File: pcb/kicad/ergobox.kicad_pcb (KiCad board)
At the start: 2 copper layers, 236 x 147 mm, 79 parts, among them SW1 SW_Push, SW10 Kailh, SW11 Kailh, SW12 Kailh, SW13 Kailh, SW14 Kailh, SW15 Kailh, SW16 Kailh, SW17 Kailh, SW18 Kailh, SW19 Kailh, SW2 SW_Push, SW20 Kailh, SW3 SW_Push, SW4 SW_Push, SW5 SW_Push, SW6 SW_Push, SW7 SW_Push, SW8 SW_Push, SW9 Kailh, U1 TLV73333PDBV, U2 RP2040, U3 W25Q128JVS, Y1 Crystal_GND24

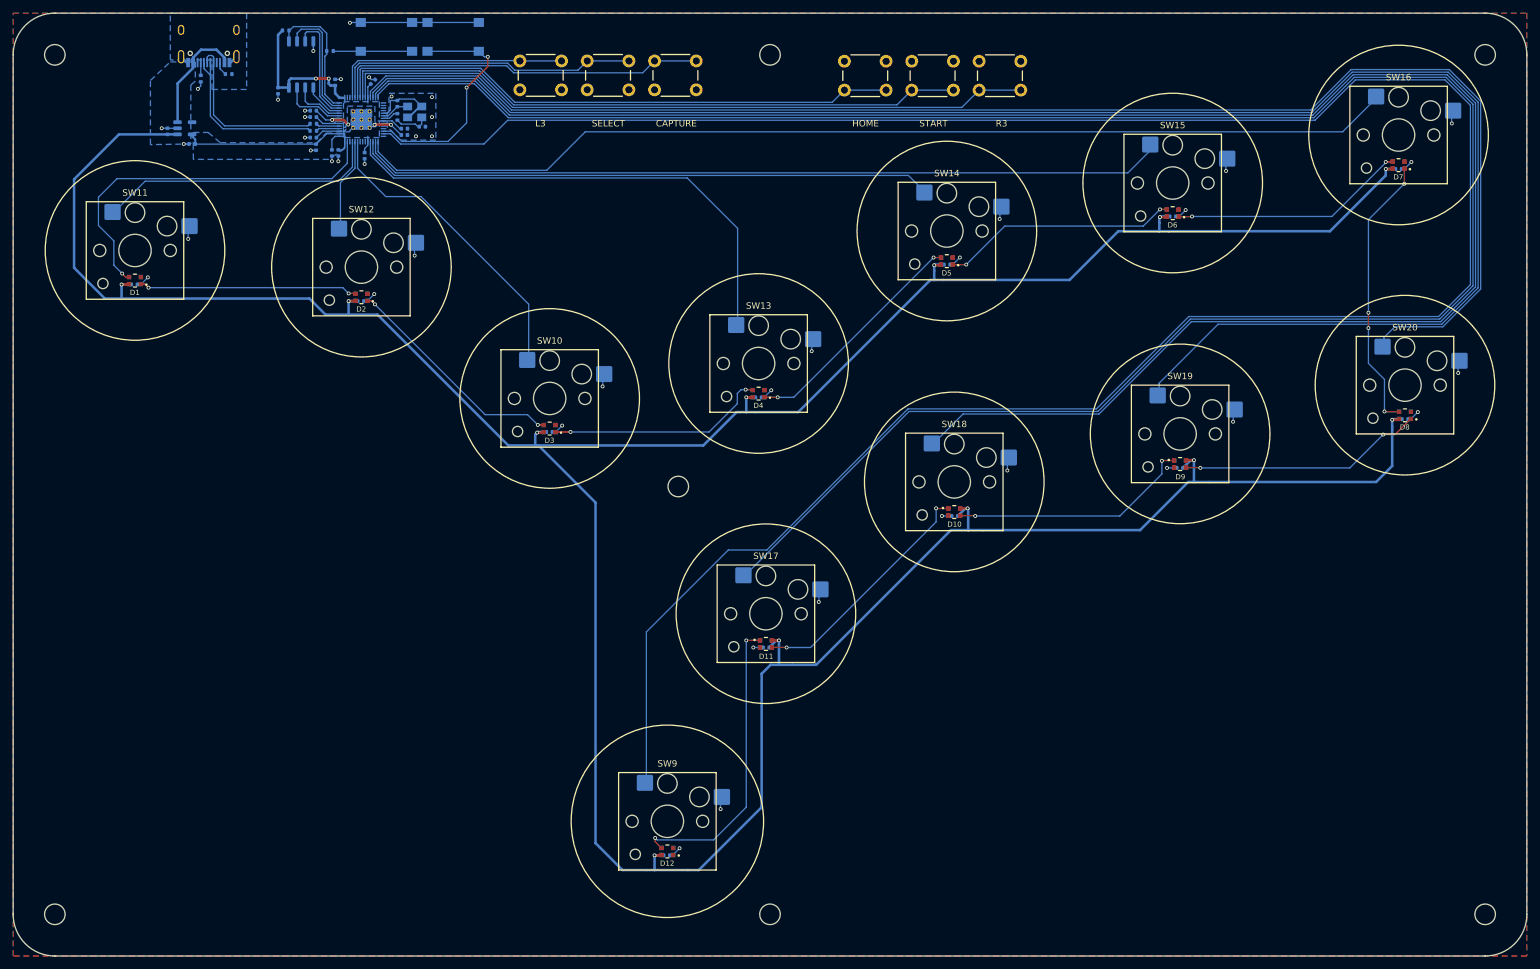
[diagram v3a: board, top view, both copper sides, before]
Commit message: chore: adds aesthetic elements to PCB design
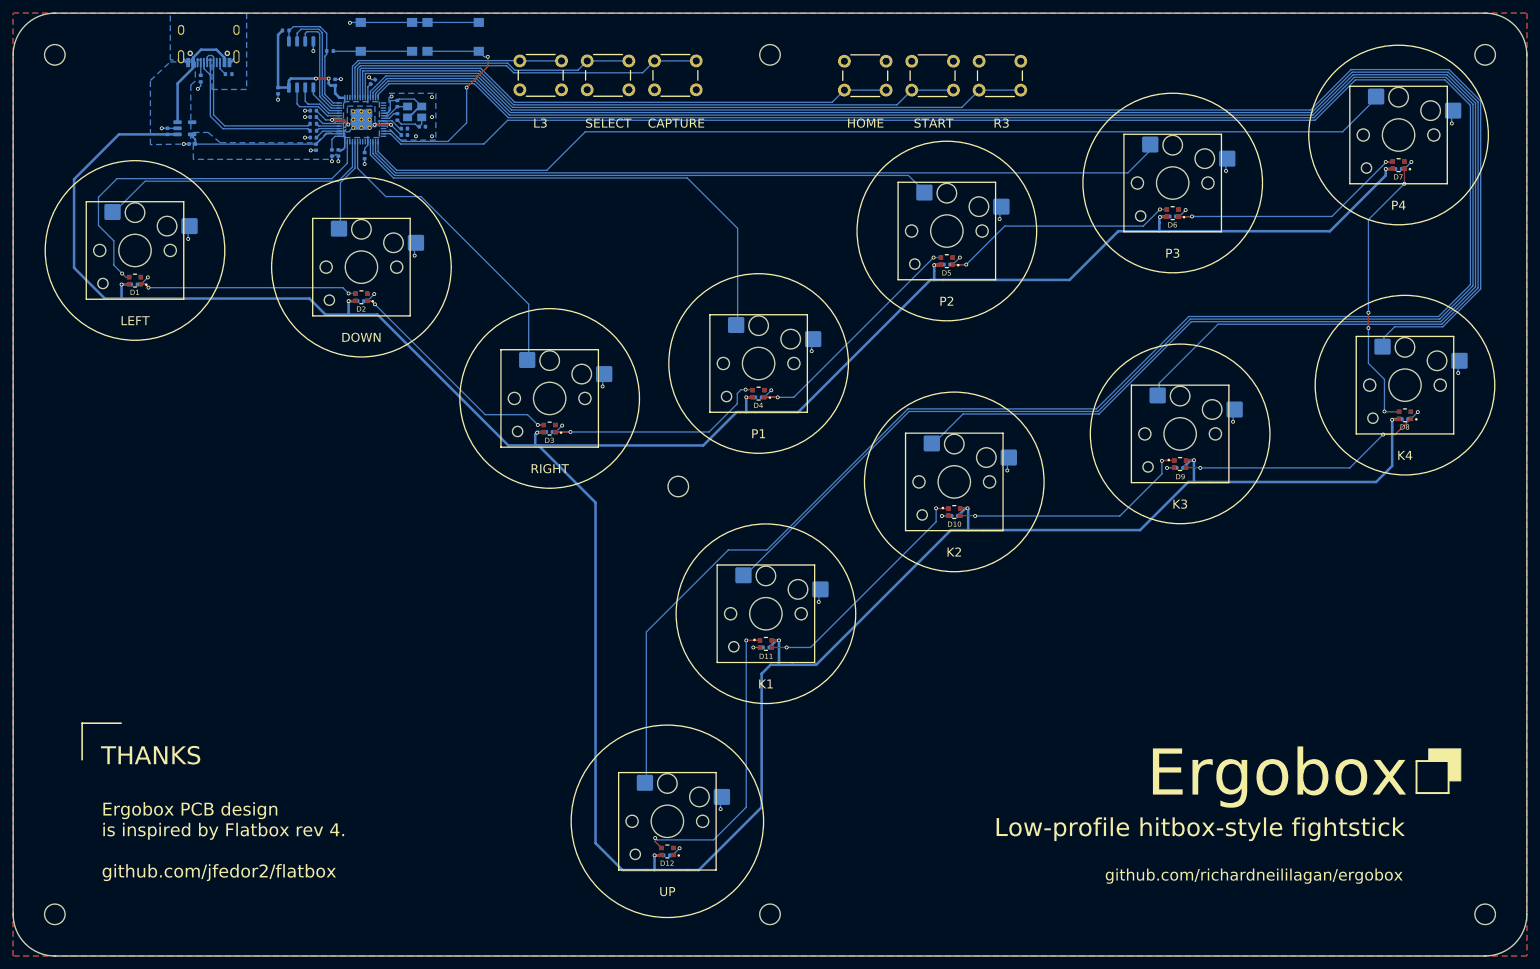
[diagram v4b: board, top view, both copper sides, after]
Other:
- board text added: "DOWN"
- board text added: "Ergobox"
- board text added: "Ergobox PCB design is inspired by Flatbox rev 4. github.com/jfedor2/flatbox"
- board text added: "K1"
- board text added: "K2"
- board text added: "K3"
- board text added: "K4"
- board text added: "LEFT"
- board text added: "Low-profile hitbox-style fightstick"
- board text added: "P1"
- board text added: "P2"
- board text added: "P3"
- board text added: "P4"
- board text added: "RIGHT"
- board text added: "THANKS"
- board text added: "UP"
- board text added: "github.com/richardneililagan/ergobox"
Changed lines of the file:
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@@
     (property "Sheetname" "")
     (attr smd)
-    (fp_text reference "SW13" (at 0 -9) (layer "F.SilkS")
+    (fp_text reference "SW13" (at 0 -9) (layer "F.SilkS") hide
       (effects (font (size 1 1) (thickness 0.15)))
     )
@@
     (property "Sheetname" "")
     (attr smd)
-    (fp_text reference "SW14" (at 0 -9) (layer "F.SilkS")
+    (fp_text reference "SW14" (at 0 -9) (layer "F.SilkS") hide
       (effects (font (size 1 1) (thickness 0.15)))
     )
@@
     (property "Sheetname" "")
     (attr smd)
-    (fp_text reference "SW10" (at 0 -9) (layer "F.SilkS")
+    (fp_text reference "SW10" (at 0 -9) (layer "F.SilkS") hide
       (effects (font (size 1 1) (thickness 0.15)))
     )
@@
     (property "Sheetname" "")
     (attr smd)
-    (fp_text reference "SW17" (at 0 -9) (layer "F.SilkS")
+    (fp_text reference "SW17" (at 0 -9) (layer "F.SilkS") hide
       (effects (font (size 1 1) (thickness 0.15)))
     )
@@
     (property "Sheetname" "")
     (attr smd)
-    (fp_text reference "SW11" (at 0 -9) (layer "F.SilkS")
+    (fp_text reference "SW11" (at 0 -9) (layer "F.SilkS") hide
       (effects (font (size 1 1) (thickness 0.15)))
     )
@@
     (property "Sheetname" "")
     (attr smd)
-    (fp_text reference "SW19" (at 0 -9) (layer "F.SilkS")
+    (fp_text reference "SW19" (at 0 -9) (layer "F.SilkS") hide
       (effects (font (size 1 1) (thickness 0.15)))
     )
@@
     (property "Sheetname" "")
     (attr smd)
-    (fp_text reference "SW20" (at 0 -9) (layer "F.SilkS")
+    (fp_text reference "SW20" (at 0 -9) (layer "F.SilkS") hide
       (effects (font (size 1 1) (thickness 0.15)))
     )
@@
     (property "Sheetname" "")
     (attr smd)
-    (fp_text reference "SW9" (at 0 -9) (layer "F.SilkS")
+    (fp_text reference "SW9" (at 0 -9) (layer "F.SilkS") hide
       (effects (font (size 1 1) (thickness 0.15)))
     )
@@
     (property "Sheetname" "")
     (attr smd)
-    (fp_text reference "SW12" (at 0 -9) (layer "F.SilkS")
+    (fp_text reference "SW12" (at 0 -9) (layer "F.SilkS") hide
       (effects (font (size 1 1) (thickness 0.15)))
     )
@@
     (property "Sheetname" "")
     (attr smd)
-    (fp_text reference "SW18" (at 0 -9) (layer "F.SilkS")
+    (fp_text reference "SW18" (at 0 -9) (layer "F.SilkS") hide
       (effects (font (size 1 1) (thickness 0.15)))
     )
@@
     (property "Sheetname" "")
     (attr smd)
-    (fp_text reference "SW16" (at 0 -9) (layer "F.SilkS")
+    (fp_text reference "SW16" (at 0 -9) (layer "F.SilkS") hide
       (effects (font (size 1 1) (thickness 0.15)))
     )
@@
     (property "Sheetname" "")
     (attr smd)
-    (fp_text reference "SW15" (at 0 -9) (layer "F.SilkS")
+    (fp_text reference "SW15" (at 0 -9) (layer "F.SilkS") hide
       (effects (font (size 1 1) (thickness 0.15)))
     )
@@
   (gr_line (start 126.1 150.9) (end 126.1 141.9) (layer "B.SilkS") (width 0.3))
   (gr_line (start 126.1 141.9) (end 117.1 141.9) (layer "B.SilkS") (width 0.3))
+  (gr_line (start 72.05 169.7) (end 72.05 164) (layer "F.SilkS") (width 0.25))
   (gr_circle (center 178.66283 146.938858) (end 192.66283 146.938858) (layer "F.SilkS") (width 0.2) (fill none))
   (gr_circle (center 278.3 111.3) (end 292.3 111.3) (layer "F.SilkS") (width 0.2) (fill none))
@@
   (gr_circle (center 144.949119 113.370757) (end 158.949119 113.370757) (layer "F.SilkS") (width 0.2) (fill none))
   (gr_circle (center 80.3 90.3) (end 94.3 90.3) (layer "F.SilkS") (width 0.2) (fill none))
+  (gr_line (start 72.05 164) (end 78.15 164) (layer "F.SilkS") (width 0.25))
+  (gr_poly
+    (pts
+      (xy 287 173)
+      (xy 285.1 173)
+      (xy 285.1 169.9)
+      (xy 282 169.9)
+      (xy 282 168)
+      (xy 287 168)
+    ) (layer "F.SilkS") (width 0.15) (fill solid))
   (gr_circle (center 206.873371 87.269642) (end 220.873371 87.269642) (layer "F.SilkS") (width 0.2) (fill none))
   (gr_circle (center 115.6 92.9) (end 129.6 92.9) (layer "F.SilkS") (width 0.2) (fill none))
@@
   (gr_circle (center 277.3 72.3) (end 291.3 72.3) (layer "F.SilkS") (width 0.2) (fill none))
   (gr_circle (center 177.526054 107.922609) (end 191.526054 107.922609) (layer "F.SilkS") (width 0.2) (fill none))
+  (gr_rect (start 280.1 169.9) (end 285.1 174.9) (layer "F.SilkS") (width 0.3) (fill none))
   (gr_circle (center 163.3 179.3) (end 178.3 179.3) (layer "F.SilkS") (width 0.2) (fill none))
   (gr_circle (center 208.030937 126.383706) (end 222.030937 126.383706) (layer "F.SilkS") (width 0.2) (fill none))
@@
     (effects (font (size 2 2) (thickness 0.25)) (justify left mirror))
   )
+  (gr_text "P2" (at 206.873371 98.269642) (layer "F.SilkS")
+    (effects (font (size 1.4 1.4) (thickness 0.35)))
+  )
+  (gr_text "DOWN" (at 115.6 103.9) (layer "F.SilkS")
+    (effects (font (size 1.4 1.4) (thickness 0.35)))
+  )
+  (gr_text "Ergobox PCB design\nis inspired by Flatbox rev 4.\n\ngithub.com/jfedor2/flatbox" (at 75.1 182.3) (layer "F.SilkS")
+    (effects (font (size 2 2) (thickness 0.15)) (justify left))
+  )
+  (gr_text "RIGHT" (at 144.949119 124.370757) (layer "F.SilkS")
+    (effects (font (size 1.4 1.4) (thickness 0.35)))
+  )
   (gr_text "R3" (at 215.4 70.5) (layer "F.SilkS")
-    (effects (font (size 1 1) (thickness 0.15)))
+    (effects (font (size 1.4 1.4) (thickness 0.15)))
+  )
+  (gr_text "Low-profile hitbox-style fightstick" (at 278.3 180.3) (layer "F.SilkS")
+    (effects (font (size 2.8 2.8) (thickness 0.32)) (justify right))
+  )
+  (gr_text "github.com/richardneililagan/ergobox" (at 278 187.7) (layer "F.SilkS")
+    (effects (font (size 1.8 1.8) (thickness 0.15)) (justify right))
+  )
+  (gr_text "Ergobox" (at 278.8 171.8) (layer "F.SilkS")
+    (effects (font (size 7.2 7.2) (thickness 1.2)) (justify right))
+  )
+  (gr_text "K3" (at 243.244252 129.898885) (layer "F.SilkS")
+    (effects (font (size 1.4 1.4) (thickness 0.35)))
+  )
+  (gr_text "K2" (at 208.030937 137.383706) (layer "F.SilkS")
+    (effects (font (size 1.4 1.4) (thickness 0.35)))
+  )
+  (gr_text "P1" (at 177.526054 118.922609) (layer "F.SilkS")
+    (effects (font (size 1.4 1.4) (thickness 0.35)))
+  )
+  (gr_text "P3" (at 242.086683 90.784821) (layer "F.SilkS")
+    (effects (font (size 1.4 1.4) (thickness 0.35)))
+  )
+  (gr_text "UP" (at 163.3 190.3) (layer "F.SilkS")
+    (effects (font (size 1.4 1.4) (thickness 0.35)))
+  )
+  (gr_text "P4" (at 277.3 83.3) (layer "F.SilkS")
+    (effects (font (size 1.4 1.4) (thickness 0.35)))
+  )
+  (gr_text "K1" (at 178.66283 157.938858) (layer "F.SilkS")
+    (effects (font (size 1.4 1.4) (thickness 0.35)))
   )
   (gr_text "HOME" (at 194.2 70.5) (layer "F.SilkS")
-    (effects (font (size 1 1) (thickness 0.15)))
+    (effects (font (size 1.4 1.4) (thickness 0.15)))
   )
   (gr_text "SELECT" (at 154.1 70.5) (layer "F.SilkS")
-    (effects (font (size 1 1) (thickness 0.15)))
+    (effects (font (size 1.4 1.4) (thickness 0.15)))
+  )
+  (gr_text "K4" (at 278.3 122.3) (layer "F.SilkS")
+    (effects (font (size 1.4 1.4) (thickness 0.35)))
+  )
+  (gr_text "THANKS" (at 75 169.1) (layer "F.SilkS")
+    (effects (font (size 2.8 2.8) (thickness 0.35)) (justify left))
   )
   (gr_text "CAPTURE" (at 164.7 70.5) (layer "F.SilkS")
-    (effects (font (size 1 1) (thickness 0.15)))
+    (effects (font (size 1.4 1.4) (thickness 0.15)))
   )
   (gr_text "START" (at 204.8 70.5) (layer "F.SilkS")
-    (effects (font (size 1 1) (thickness 0.15)))
+    (effects (font (size 1.4 1.4) (thickness 0.15)))
+  )
+  (gr_text "LEFT" (at 80.3 101.3) (layer "F.SilkS")
+    (effects (font (size 1.4 1.4) (thickness 0.35)))
   )
   (gr_text "L3" (at 143.5 70.5) (layer "F.SilkS")
-    (effects (font (size 1 1) (thickness 0.15)))
+    (effects (font (size 1.4 1.4) (thickness 0.15)))
   )
   (segment (start 112.828851 69.9505) (end 113.5505 70.672149) (width 0.4) (layer "F.Cu") (net 1))

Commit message: chore: adjusts schematic and PCB metadata for BOM/POS export
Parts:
- C17, C18, C19, C20, C21, C22, C23, C24, C25, C26, C27, C28: value 100nF -> 100n

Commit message: chore: adds make command for generating pcb fab artifacts
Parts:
- renumbered SW9 to KSW1, SW18 to KSW10, SW19 to KSW11, SW20 to KSW12, SW10 to KSW2, SW11 to KSW3, SW12 to KSW4, SW13 to KSW5, SW14 to KSW6, SW15 to KSW7, SW16 to KSW8, SW17 to KSW9
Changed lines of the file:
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@@
     (descr "Kailh Choc keyswitch CPG1350 V1 CPG1353 V2 Hotswap")
     (tags "Kailh Choc Keyswitch Switch CPG1350 V1 CPG1353 V2 Hotswap Cutout")
+    (property "JLCPCB_IGNORE" "")
     (property "Sheetfile" "ergobox.kicad_sch")
     (property "Sheetname" "")
     (attr smd)
-    (fp_text reference "SW13" (at 0 -9) (layer "F.SilkS") hide
+    (fp_text reference "KSW5" (at 0 -9) (layer "F.SilkS") hide
       (effects (font (size 1 1) (thickness 0.15)))
     )
@@
     (descr "Kailh Choc keyswitch CPG1350 V1 CPG1353 V2 Hotswap")
     (tags "Kailh Choc Keyswitch Switch CPG1350 V1 CPG1353 V2 Hotswap Cutout")
+    (property "JLCPCB_IGNORE" "")
     (property "Sheetfile" "ergobox.kicad_sch")
     (property "Sheetname" "")
     (attr smd)
-    (fp_text reference "SW14" (at 0 -9) (layer "F.SilkS") hide
+    (fp_text reference "KSW6" (at 0 -9) (layer "F.SilkS") hide
       (effects (font (size 1 1) (thickness 0.15)))
     )
@@
     (descr "Kailh Choc keyswitch CPG1350 V1 CPG1353 V2 Hotswap")
     (tags "Kailh Choc Keyswitch Switch CPG1350 V1 CPG1353 V2 Hotswap Cutout")
+    (property "JLCPCB_IGNORE" "true")
     (property "Sheetfile" "ergobox.kicad_sch")
     (property "Sheetname" "")
     (attr smd)
-    (fp_text reference "SW10" (at 0 -9) (layer "F.SilkS") hide
+    (fp_text reference "KSW2" (at 0 -9) (layer "F.SilkS") hide
       (effects (font (size 1 1) (thickness 0.15)))
     )
@@
     (descr "Kailh Choc keyswitch CPG1350 V1 CPG1353 V2 Hotswap")
     (tags "Kailh Choc Keyswitch Switch CPG1350 V1 CPG1353 V2 Hotswap Cutout")
+    (property "JLCPCB_IGNORE" "")
     (property "Sheetfile" "ergobox.kicad_sch")
     (property "Sheetname" "")
     (attr smd)
-    (fp_text reference "SW17" (at 0 -9) (layer "F.SilkS") hide
+    (fp_text reference "KSW9" (at 0 -9) (layer "F.SilkS") hide
       (effects (font (size 1 1) (thickness 0.15)))
     )
@@
     (descr "Kailh Choc keyswitch CPG1350 V1 CPG1353 V2 Hotswap")
     (tags "Kailh Choc Keyswitch Switch CPG1350 V1 CPG1353 V2 Hotswap Cutout")
+    (property "JLCPCB_IGNORE" "")
     (property "Sheetfile" "ergobox.kicad_sch")
     (property "Sheetname" "")
     (attr smd)
-    (fp_text reference "SW11" (at 0 -9) (layer "F.SilkS") hide
+    (fp_text reference "KSW3" (at 0 -9) (layer "F.SilkS") hide
       (effects (font (size 1 1) (thickness 0.15)))
     )
@@
     (descr "Kailh Choc keyswitch CPG1350 V1 CPG1353 V2 Hotswap")
     (tags "Kailh Choc Keyswitch Switch CPG1350 V1 CPG1353 V2 Hotswap Cutout")
+    (property "JLCPCB_IGNORE" "")
     (property "Sheetfile" "ergobox.kicad_sch")
     (property "Sheetname" "")
     (attr smd)
-    (fp_text reference "SW19" (at 0 -9) (layer "F.SilkS") hide
+    (fp_text reference "KSW11" (at 0 -9) (layer "F.SilkS") hide
       (effects (font (size 1 1) (thickness 0.15)))
     )
@@
     (descr "Kailh Choc keyswitch CPG1350 V1 CPG1353 V2 Hotswap")
     (tags "Kailh Choc Keyswitch Switch CPG1350 V1 CPG1353 V2 Hotswap Cutout")
+    (property "JLCPCB_IGNORE" "")
     (property "Sheetfile" "ergobox.kicad_sch")
     (property "Sheetname" "")
     (attr smd)
-    (fp_text reference "SW20" (at 0 -9) (layer "F.SilkS") hide
+    (fp_text reference "KSW12" (at 0 -9) (layer "F.SilkS") hide
       (effects (font (size 1 1) (thickness 0.15)))
     )
@@
     (descr "Kailh Choc keyswitch CPG1350 V1 CPG1353 V2 Hotswap")
     (tags "Kailh Choc Keyswitch Switch CPG1350 V1 CPG1353 V2 Hotswap Cutout")
+    (property "JLCPCB_IGNORE" "true")
     (property "Sheetfile" "ergobox.kicad_sch")
     (property "Sheetname" "")
     (attr smd)
-    (fp_text reference "SW9" (at 0 -9) (layer "F.SilkS") hide
+    (fp_text reference "KSW1" (at 0 -9) (layer "F.SilkS") hide
       (effects (font (size 1 1) (thickness 0.15)))
     )
@@
     (descr "Kailh Choc keyswitch CPG1350 V1 CPG1353 V2 Hotswap")
     (tags "Kailh Choc Keyswitch Switch CPG1350 V1 CPG1353 V2 Hotswap Cutout")
+    (property "JLCPCB_IGNORE" "")
     (property "Sheetfile" "ergobox.kicad_sch")
     (property "Sheetname" "")
     (attr smd)
-    (fp_text reference "SW12" (at 0 -9) (layer "F.SilkS") hide
+    (fp_text reference "KSW4" (at 0 -9) (layer "F.SilkS") hide
       (effects (font (size 1 1) (thickness 0.15)))
     )
@@
     (descr "Kailh Choc keyswitch CPG1350 V1 CPG1353 V2 Hotswap")
     (tags "Kailh Choc Keyswitch Switch CPG1350 V1 CPG1353 V2 Hotswap Cutout")
+    (property "JLCPCB_IGNORE" "")
     (property "Sheetfile" "ergobox.kicad_sch")
     (property "Sheetname" "")
     (attr smd)
-    (fp_text reference "SW18" (at 0 -9) (layer "F.SilkS") hide
+    (fp_text reference "KSW10" (at 0 -9) (layer "F.SilkS") hide
       (effects (font (size 1 1) (thickness 0.15)))
     )
@@
     (descr "Kailh Choc keyswitch CPG1350 V1 CPG1353 V2 Hotswap")
     (tags "Kailh Choc Keyswitch Switch CPG1350 V1 CPG1353 V2 Hotswap Cutout")
+    (property "JLCPCB_IGNORE" "")
     (property "Sheetfile" "ergobox.kicad_sch")
     (property "Sheetname" "")
     (attr smd)
-    (fp_text reference "SW16" (at 0 -9) (layer "F.SilkS") hide
+    (fp_text reference "KSW8" (at 0 -9) (layer "F.SilkS") hide
       (effects (font (size 1 1) (thickness 0.15)))
     )
@@
     (descr "Kailh Choc keyswitch CPG1350 V1 CPG1353 V2 Hotswap")
     (tags "Kailh Choc Keyswitch Switch CPG1350 V1 CPG1353 V2 Hotswap Cutout")
+    (property "JLCPCB_IGNORE" "")
     (property "Sheetfile" "ergobox.kicad_sch")
     (property "Sheetname" "")
     (attr smd)
-    (fp_text reference "SW15" (at 0 -9) (layer "F.SilkS") hide
+    (fp_text reference "KSW7" (at 0 -9) (layer "F.SilkS") hide
       (effects (font (size 1 1) (thickness 0.15)))
     )
@@
     (descr "Capacitor SMD 0402 (1005 Metric), square (rectangular) end terminal, IPC_7351 nominal, (Body size source: IPC-SM-782 page 76, https://www.pcb-3d.com/wordpress/wp-content/uploads/ipc-sm-782a_amendment_1_and_2.pdf), generated with kicad-footprint-generator")
     (tags "capacitor")
+    (property "JLCPCB_CORRECTION" "0;0;90")
     (property "LCSC" "C1525")
     (property "Sheetfile" "ergobox.kicad_sch")
@@
     (descr "SMD Crystal SERIES SMD3225/4 http://www.txccrystal.com/images/pdf/7m-accuracy.pdf, 3.2x2.5mm^2 package")
     (tags "SMD SMT crystal")
+    (property "JLCPCB_CORRECTION" "0;0;180")
     (property "LCSC" "C9002")
     (property "Sheetfile" "ergobox.kicad_sch")
@@
     (descr "SOIC, 8 Pin (http://www.winbond.com/resource-files/w25q32jv%20revg%2003272018%20plus.pdf#page=68), generated with kicad-footprint-generator ipc_gullwing_generator.py")
     (tags "SOIC SO")
+    (property "JLCPCB_CORRECTION" "0;0;-90")
     (property "LCSC" "C97521")
     (property "Sheetfile" "ergobox.kicad_sch")
@@
   (footprint "USB-C:HRO-TYPE-C-31-M-12" locked (layer "B.Cu")
     (at 91.8 53.315)
+    (property "JLCPCB_CORRECTION" "0;5.25;180")
     (property "LCSC" "C165948")
     (property "Sheetfile" "ergobox.kicad_sch")
